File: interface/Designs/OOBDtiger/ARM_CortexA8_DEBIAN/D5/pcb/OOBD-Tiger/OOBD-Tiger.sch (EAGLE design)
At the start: 123 parts, among them IC1 ADM3053M, IC2 ADM3053M, IC4 DS3231, U1 SY6280, U10 MP1482DS, U2 SN65HVD230(SO8), U3 SY6280, U6 SN65HVD230(SO8)

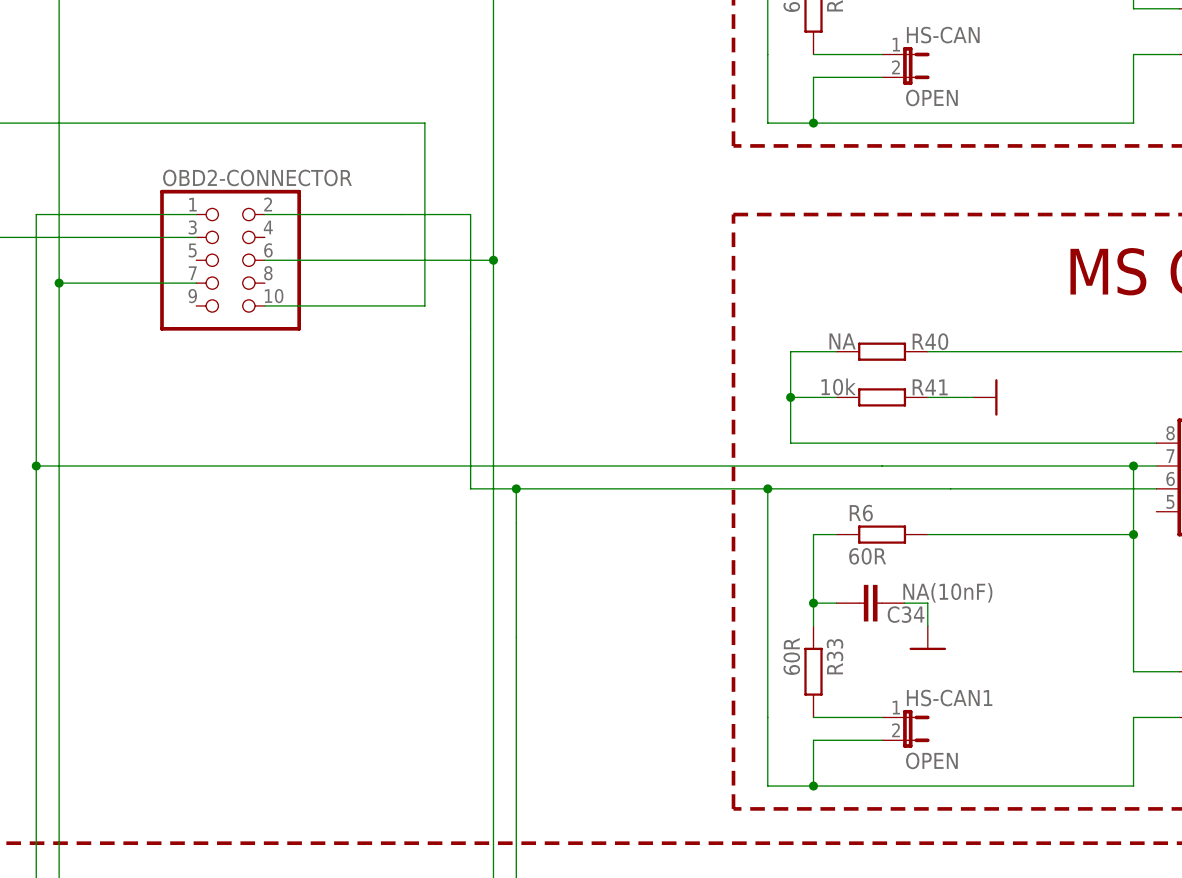
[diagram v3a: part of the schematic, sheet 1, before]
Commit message: Platzierung abgeschlossen, Anschluss LED3 und Bauteilwert L2 offen
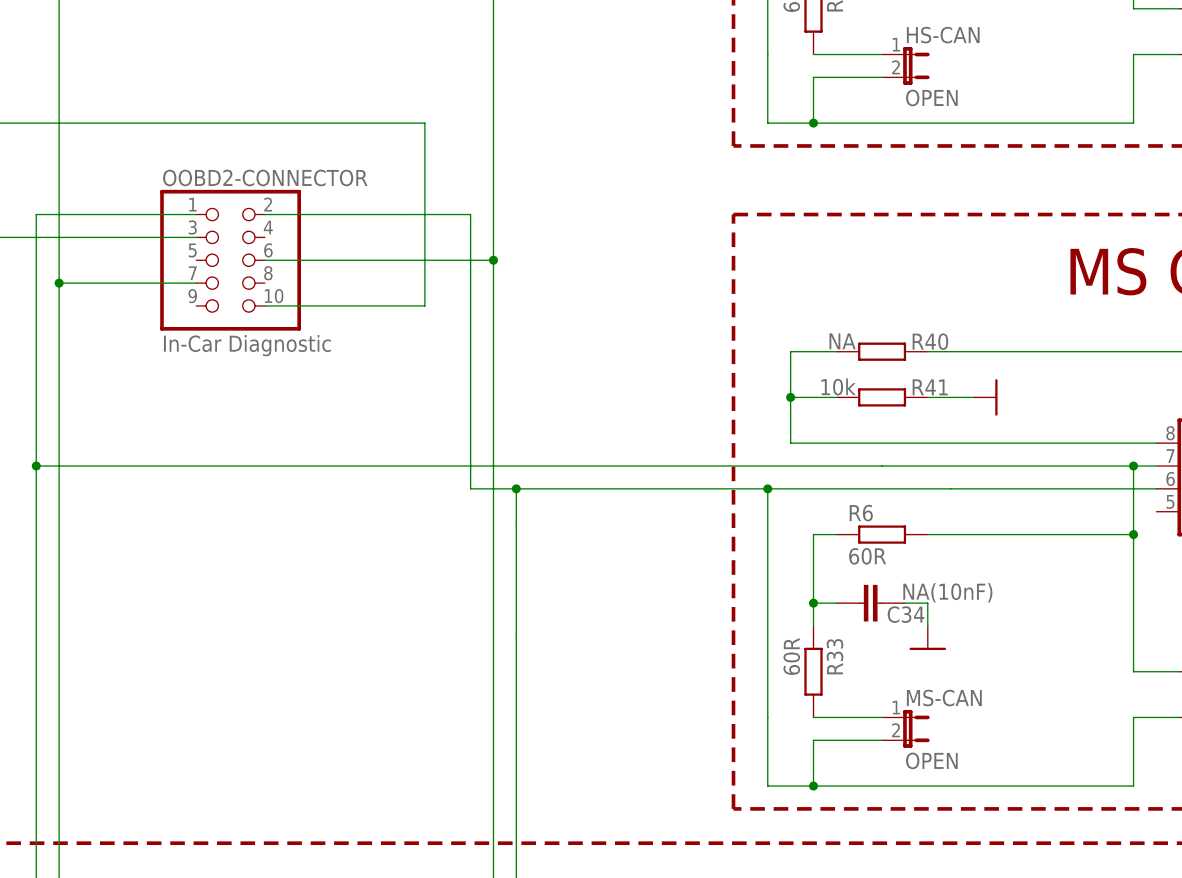
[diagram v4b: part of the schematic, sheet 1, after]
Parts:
- BAT2: value (none) -> 3,6V
- OOBD2-CONNECTOR: value (none) -> In-Car Diagnostic
- OOBDPICAN: value (none) -> Bridge to PICAN
- TLV320AIC3107: value (none) -> Audio-Amplifier
- renumbered HS-CAN1 to MS-CAN, JP1 to OOBDPICAN, OBD2-CONNECTOR to OOBD2-CONNECTOR
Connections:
- removed net PMIC_POWER_EN: AM3352-SOM-EVB-PLATFORM.PMIC_POWER_EN
- net P3_20/LED2: now also AM3352-SOM-EVB-PLATFORM.P3_20/LED2
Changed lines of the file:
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@@
 <?xml version="1.0" encoding="utf-8"?>
 <!DOCTYPE eagle SYSTEM "eagle.dtd">
-<eagle version="6.4">
+<eagle version="7.6.0">
 <drawing>
 <settings>
@@
 <setting verticaltext="up"/>
 </settings>
-<grid distance="0.1" unitdist="inch" unit="inch" style="lines" multiple="1" display="yes" altdistance="0.01" altunitdist="inch" altunit="inch"/>
+<grid distance="0.1" unitdist="inch" unit="inch" style="lines" multiple="1" display="no" altdistance="0.01" altunitdist="inch" altunit="inch"/>
 <layers>
 <layer number="1" name="Top" color="4" fill="1" visible="no" active="no"/>
@@
 <part name="GND5" library="supply1" deviceset="GND" device="" value=""/>
 <part name="R7" library="rcl" deviceset="R-EU_" device="R0603" value="NA"/>
-<part name="OBD2-CONNECTOR" library="pinhead" deviceset="PINHD-2X5" device="/90"/>
+<part name="OOBD2-CONNECTOR" library="pinhead" deviceset="PINHD-2X5" device="/90" value="In-Car Diagnostic"/>
 <part name="R8" library="resistor" deviceset="R-EU_" device="R0603" value="10K">
 <attribute name="MANEX" value="110-0002014 "/>
@@
 <attribute name="MANEX" value="123-0001115 "/>
 </part>
-<part name="TLV320AIC3107" library="TLV320AIC3107" deviceset="TLV320AIC3107" device=""/>
+<part name="TLV320AIC3107" library="TLV320AIC3107" deviceset="TLV320AIC3107" device="" value="Audio-Amplifier"/>
 <part name="R12" library="resistor" deviceset="R-EU_" device="R0603" value="0"/>
 <part name="R13" library="resistor" deviceset="R-EU_" device="R0603" value="0"/>
@@
 <part name="GND11" library="supply1" deviceset="GND" device=""/>
 <part name="GND16" library="supply1" deviceset="GND" device=""/>
-<part name="BAT2" library="SparkFun" deviceset="BATTERY" device="12PTH"/>
+<part name="BAT2" library="SparkFun" deviceset="BATTERY" device="12PTH" value="3,6V"/>
 <part name="USB_HOST" library="OLIMEX_CONNECTORS" deviceset="USB_SHIELD" device="1" value="USB_A_VERTICAL"/>
 <part name="L5" library="rcl" deviceset="L-US" device="L0805_5MIL_DWS" value="FB0805/600R/2A"/>
@@
 <part name="GND51" library="supply1" deviceset="GND" device="" value=""/>
 <part name="GND52" library="supply1" deviceset="GND" device="" value=""/>
-<part name="HS-CAN1" library="SparkFun" deviceset="JUMPER-2" device="SMD-NO" value="OPEN"/>
+<part name="MS-CAN" library="SparkFun" deviceset="JUMPER-2" device="SMD-NO" value="OPEN"/>
 <part name="R6" library="resistor" deviceset="R-EU_" device="R0603" value="60R"/>
 <part name="R33" library="resistor" deviceset="R-EU_" device="R0603" value="60R"/>
@@
 <part name="GND54" library="supply1" deviceset="GND" device="" value=""/>
 <part name="GND55" library="supply1" deviceset="GND" device="" value=""/>
-<part name="JP1" library="jumper" deviceset="JP3Q" device=""/>
+<part name="OOBDPICAN" library="jumper" deviceset="JP3Q" device="" value="Bridge to PICAN"/>
 <part name="GND57" library="supply1" deviceset="GND" device="" value=""/>
 <part name="P+9" library="supply1" deviceset="+5V" device=""/>
@@
 <attribute name="VALUE" x="136.779" y="231.394" size="1.778" layer="96" rot="MR0"/>
 </instance>
-<instance part="OBD2-CONNECTOR" gate="A" x="66.04" y="167.64"/>
+<instance part="OOBD2-CONNECTOR" gate="A" x="66.04" y="167.64"/>
 <instance part="GND6" gate="1" x="15.24" y="162.56"/>
 <instance part="P+2" gate="1" x="15.24" y="190.5"/>
@@
 <instance part="GND51" gate="1" x="144.78" y="198.12"/>
 <instance part="GND52" gate="1" x="195.58" y="182.88"/>
-<instance part="HS-CAN1" gate="A" x="142.24" y="116.84" rot="R270"/>
+<instance part="MS-CAN" gate="A" x="142.24" y="116.84" rot="R270"/>
 <instance part="R6" gate="G$1" x="139.7" y="137.16"/>
 <instance part="R33" gate="G$1" x="132.08" y="121.92" rot="R270"/>
@@
 </segment>
 <segment>
-<pinref part="OBD2-CONNECTOR" gate="A" pin="3"/>
+<pinref part="OOBD2-CONNECTOR" gate="A" pin="3"/>
 <wire x1="63.5" y1="170.18" x2="15.24" y2="170.18" width="0.1524" layer="91"/>
 <pinref part="GND6" gate="1" pin="GND"/>
@@
 <wire x1="170.18" y1="142.24" x2="147.32" y2="142.24" width="0.1524" layer="91"/>
 <wire x1="147.32" y1="142.24" x2="127" y2="142.24" width="0.1524" layer="91"/>
-<pinref part="OBD2-CONNECTOR" gate="A" pin="2"/>
+<pinref part="OOBD2-CONNECTOR" gate="A" pin="2"/>
 <wire x1="127" y1="142.24" x2="99.06" y2="142.24" width="0.1524" layer="91"/>
 <wire x1="99.06" y1="142.24" x2="93.98" y2="142.24" width="0.1524" layer="91"/>
@@
 <wire x1="127" y1="109.22" x2="127" y2="116.84" width="0.1524" layer="91"/>
 <wire x1="127" y1="116.84" x2="127" y2="142.24" width="0.1524" layer="91"/>
-<pinref part="HS-CAN1" gate="A" pin="2"/>
+<pinref part="MS-CAN" gate="A" pin="2"/>
 <wire x1="139.7" y1="114.3" x2="132.08" y2="114.3" width="0.1524" layer="91"/>
 <wire x1="132.08" y1="114.3" x2="132.08" y2="109.22" width="0.1524" layer="91"/>
@@
 <pinref part="IC2" gate="G$1" pin="CAN_H"/>
 <wire x1="209.55" y1="44.45" x2="210.82" y2="44.45" width="0.1524" layer="91"/>
-<pinref part="OBD2-CONNECTOR" gate="A" pin="1"/>
+<pinref part="OOBD2-CONNECTOR" gate="A" pin="1"/>
 <wire x1="63.5" y1="172.72" x2="45.72" y2="172.72" width="0.1524" layer="91"/>
 <wire x1="45.72" y1="172.72" x2="45.72" y2="144.78" width="0.1524" layer="91"/>
@@
 <wire x1="127" y1="215.9" x2="96.52" y2="215.9" width="0.1524" layer="91"/>
 <wire x1="96.52" y1="200.66" x2="96.52" y2="215.9" width="0.1524" layer="91"/>
-<pinref part="OBD2-CONNECTOR" gate="A" pin="6"/>
+<pinref part="OOBD2-CONNECTOR" gate="A" pin="6"/>
 <wire x1="96.52" y1="167.64" x2="96.52" y2="198.12" width="0.1524" layer="91"/>
 <wire x1="71.12" y1="167.64" x2="96.52" y2="167.64" width="0.1524" layer="91"/>
@@
 <net name="+12V" class="0">
 <segment>
-<pinref part="OBD2-CONNECTOR" gate="A" pin="10"/>
+<pinref part="OOBD2-CONNECTOR" gate="A" pin="10"/>
 <wire x1="71.12" y1="162.56" x2="88.9" y2="162.56" width="0.1524" layer="91"/>
 <wire x1="88.9" y1="162.56" x2="88.9" y2="182.88" width="0.1524" layer="91"/>
@@
 <wire x1="109.22" y1="218.44" x2="48.26" y2="218.44" width="0.1524" layer="91"/>
 <wire x1="48.26" y1="218.44" x2="48.26" y2="165.1" width="0.1524" layer="91"/>
-<pinref part="OBD2-CONNECTOR" gate="A" pin="7"/>
+<pinref part="OOBD2-CONNECTOR" gate="A" pin="7"/>
 <junction x="48.26" y="165.1"/>
 <wire x1="48.26" y1="165.1" x2="63.5" y2="165.1" width="0.1524" layer="91"/>
@@
 <segment>
 <pinref part="R33" gate="G$1" pin="2"/>
-<pinref part="HS-CAN1" gate="A" pin="1"/>
+<pinref part="MS-CAN" gate="A" pin="1"/>
 <wire x1="132.08" y1="116.84" x2="139.7" y2="116.84" width="0.1524" layer="91"/>
 </segment>
@@
 <instance part="GND32" gate="1" x="190.5" y="73.66" rot="MR0"/>
 <instance part="SUPPLY8" gate="G$1" x="276.86" y="167.64"/>
-<instance part="JP1" gate="B" x="124.46" y="35.56" rot="R270"/>
+<instance part="OOBDPICAN" gate="B" x="124.46" y="35.56" rot="R270"/>
 <instance part="GND57" gate="1" x="111.76" y="25.4" rot="MR0"/>
 <instance part="P+9" gate="1" x="111.76" y="45.72" smashed="yes" rot="MR0">
@@
 </segment>
 <segment>
-<pinref part="JP1" gate="B" pin="5"/>
+<pinref part="OOBDPICAN" gate="B" pin="5"/>
 <pinref part="GND57" gate="1" pin="GND"/>
 <wire x1="116.84" y1="33.02" x2="111.76" y2="33.02" width="0.1524" layer="91"/>
@@
 </segment>
 <segment>
-<pinref part="JP1" gate="B" pin="1"/>
+<pinref part="OOBDPICAN" gate="B" pin="1"/>
 <pinref part="P+9" gate="1" pin="+5V"/>
 <wire x1="116.84" y1="38.1" x2="111.76" y2="38.1" width="0.1524" layer="91"/>
@@
 </segment>
 <segment>
-<pinref part="JP1" gate="B" pin="2"/>
+<pinref part="OOBDPICAN" gate="B" pin="2"/>
 <wire x1="132.08" y1="38.1" x2="231.14" y2="38.1" width="0.1524" layer="91"/>
 <label x="231.14" y="38.1" size="1.778" layer="95" xref="yes"/>
@@
 </segment>
 <segment>
-<pinref part="JP1" gate="B" pin="4"/>
+<pinref part="OOBDPICAN" gate="B" pin="4"/>
 <wire x1="132.08" y1="35.56" x2="231.14" y2="35.56" width="0.1524" layer="91"/>
 <label x="231.14" y="35.56" size="1.778" layer="95" xref="yes"/>
@@
 </segment>
 </net>
-<net name="PMIC_POWER_EN" class="0">
-<segment>
-<wire x1="190.5" y1="195.58" x2="152.4" y2="195.58" width="0.1524" layer="91"/>
-<label x="165.1" y="195.834" size="1.778" layer="95" ratio="15"/>
-<pinref part="AM3352-SOM-EVB-PLATFORM" gate="G$1" pin="PMIC_POWER_EN"/>
-</segment>
-</net>
 <net name="MS-CAN_RS" class="0">
 <segment>
@@
 <wire x1="215.9" y1="121.92" x2="218.44" y2="124.46" width="0.1524" layer="91"/>
 <label x="165.1" y="121.92" size="1.778" layer="95"/>
+</segment>
+</net>
+<net name="P3_20/LED2" class="0">
+<segment>
+<wire x1="86.36" y1="121.92" x2="63.5" y2="121.92" width="0.1524" layer="91"/>
+<label x="63.5" y="121.92" size="1.778" layer="95"/>
+<pinref part="AM3352-SOM-EVB-PLATFORM" gate="G$1" pin="P3_20/LED2"/>
+<junction x="86.36" y="121.92"/>
 </segment>
 </net>
@@
 <wire x1="180.34" y1="220.98" x2="180.34" y2="226.06" width="0.1524" layer="91"/>
 <wire x1="180.34" y1="226.06" x2="157.48" y2="226.06" width="0.1524" layer="91"/>
-<label x="157.48" y="225.171" size="1.778" layer="95" ratio="15"/>
+<label x="157.48" y="227.711" size="1.778" layer="95" ratio="15"/>
 <pinref part="R49" gate="G$1" pin="1"/>
 </segment>
@@
 <segment>
 <wire x1="83.82" y1="205.74" x2="96.52" y2="205.74" width="0.1524" layer="91"/>
-<label x="87.63" y="205.105" size="1.778" layer="95" ratio="15"/>
+<label x="85.09" y="205.105" size="1.778" layer="95" ratio="15"/>
 <pinref part="R54" gate="G$1" pin="1"/>
 </segment>

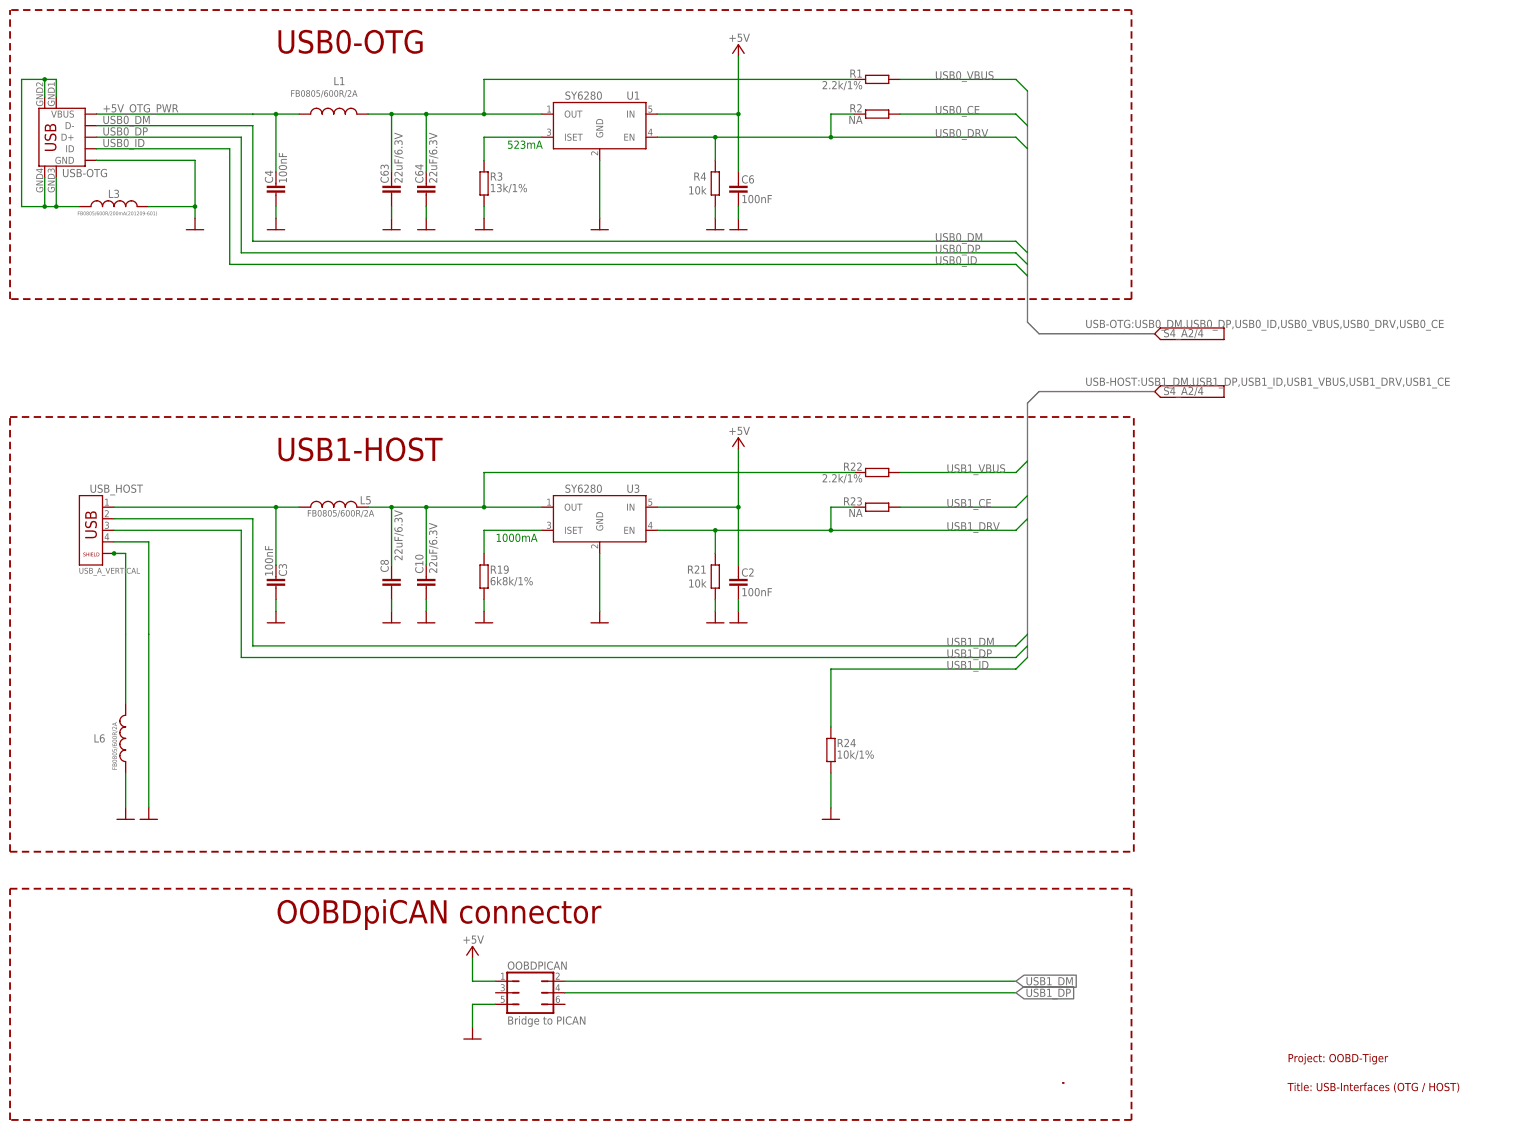
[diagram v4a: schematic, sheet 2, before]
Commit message: small modifications on schematics/board (signal re-alignment only)
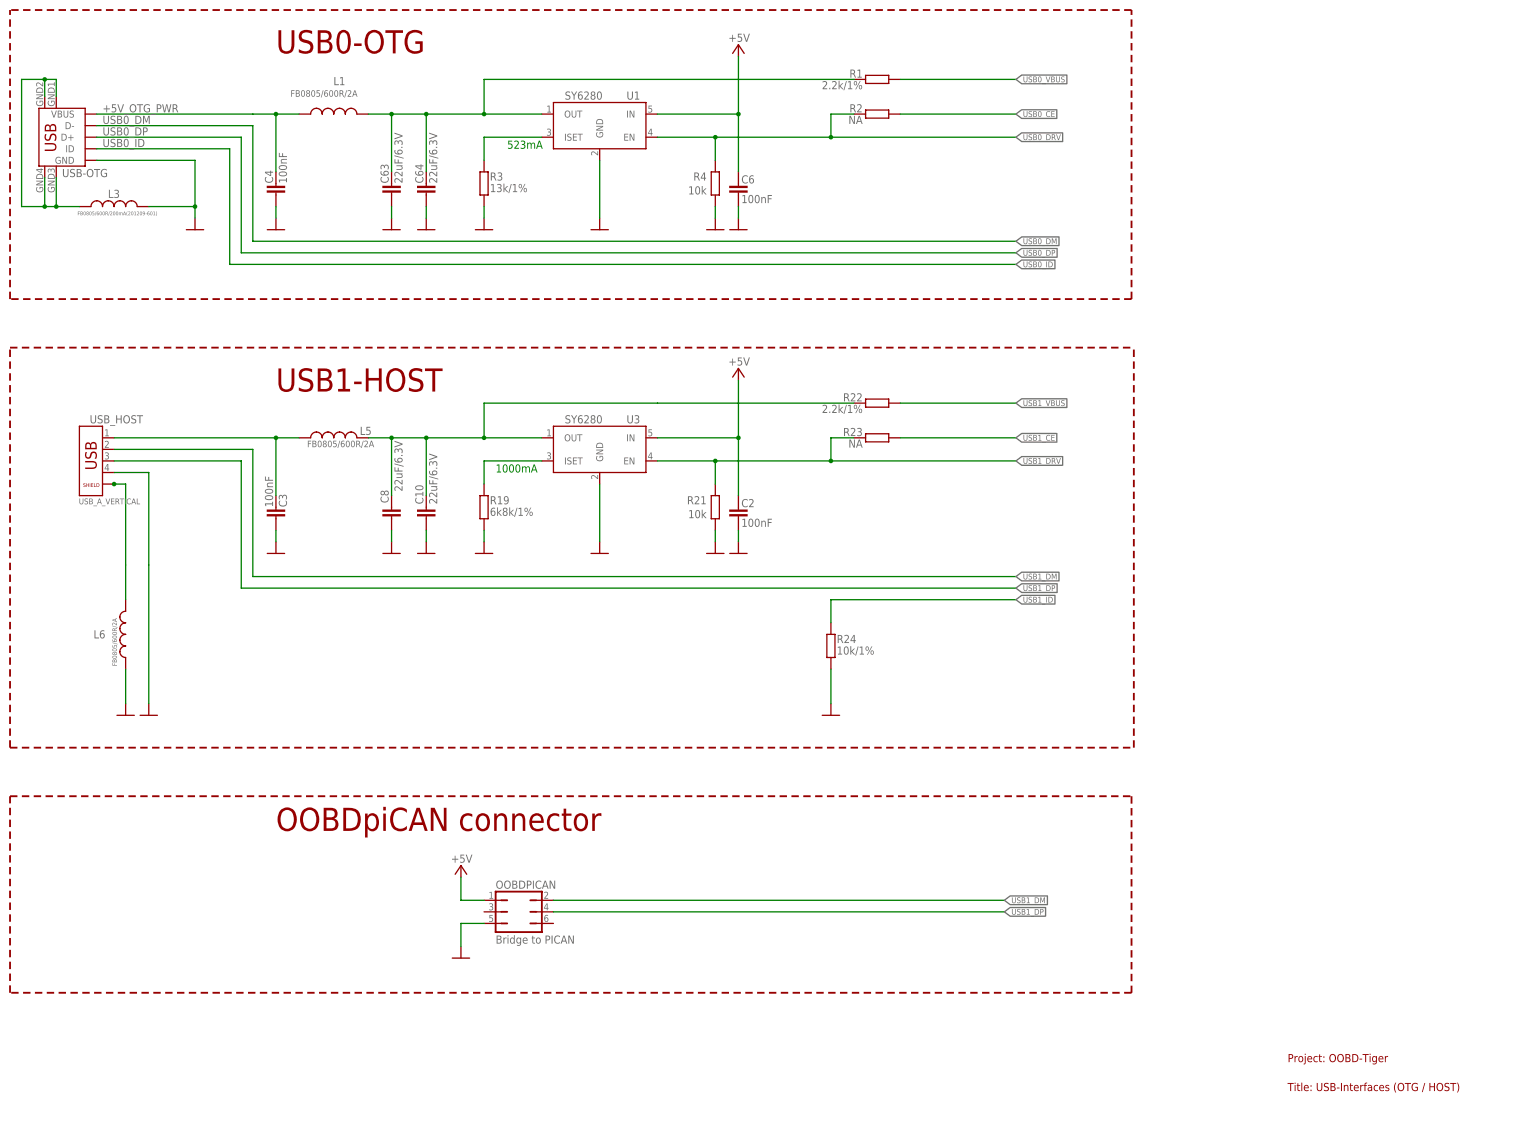
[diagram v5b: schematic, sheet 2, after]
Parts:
- removed 5V_E: Close, jumper:SJ
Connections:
- net P3_20/LED2 renamed LED2
- removed net N$12: 5V_E.1, C53.1, C54.1, C55.1, C56.1, L11.2, R70.2
- removed net P3_21/LED3: R48.1
- new net LED1: AM3352-SOM-EVB-PLATFORM.P3_18/LED1, R48.1
- net +5V: now also C53.1, C54.1, C55.1, C56.1, L11.2, R70.2; no longer 5V_E.2
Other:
- moved on the sheet: BAT2, C10, C2, C3, C48, C8, IC4, L5, L6, OOBDPICAN, R19, R20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
